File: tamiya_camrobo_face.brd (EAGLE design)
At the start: 60 x 30 mm, 21 parts, among them J4 AUDIO_JACK_3.5MM_KIT

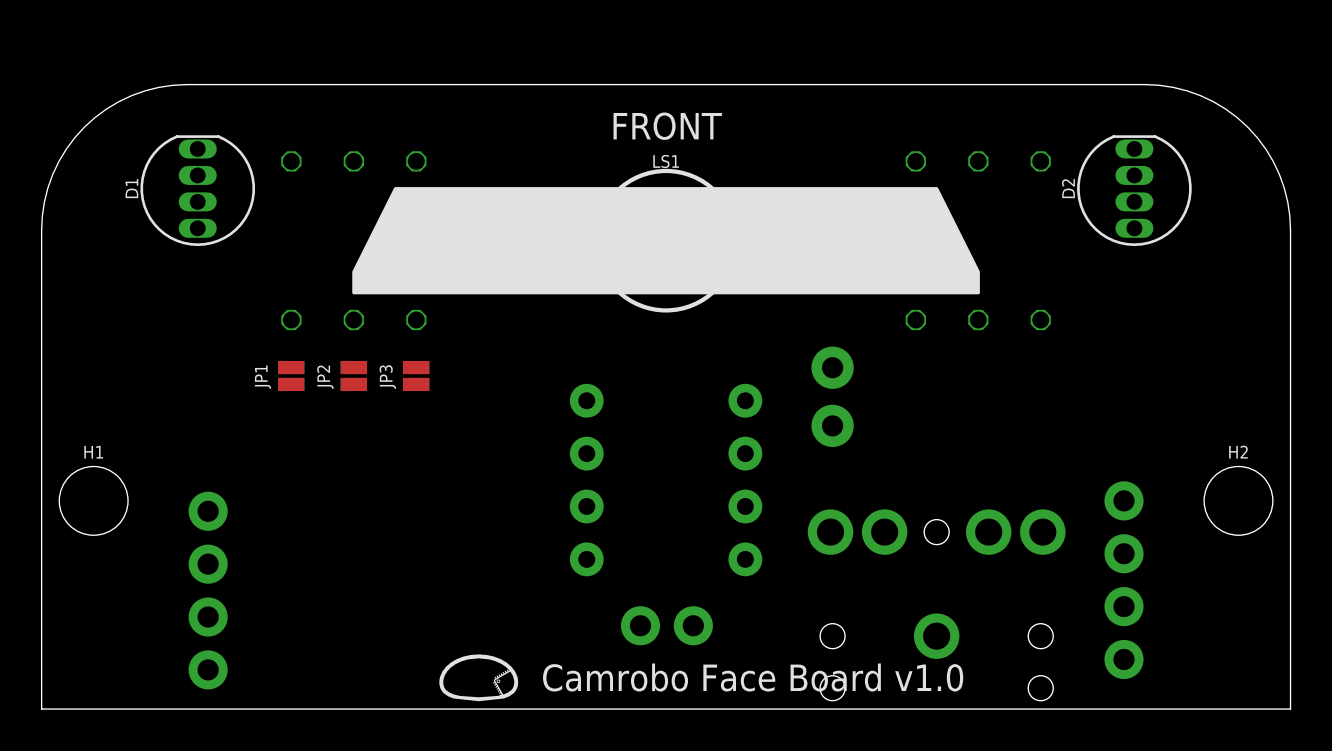
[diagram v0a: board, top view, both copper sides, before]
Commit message: exchange led and amp
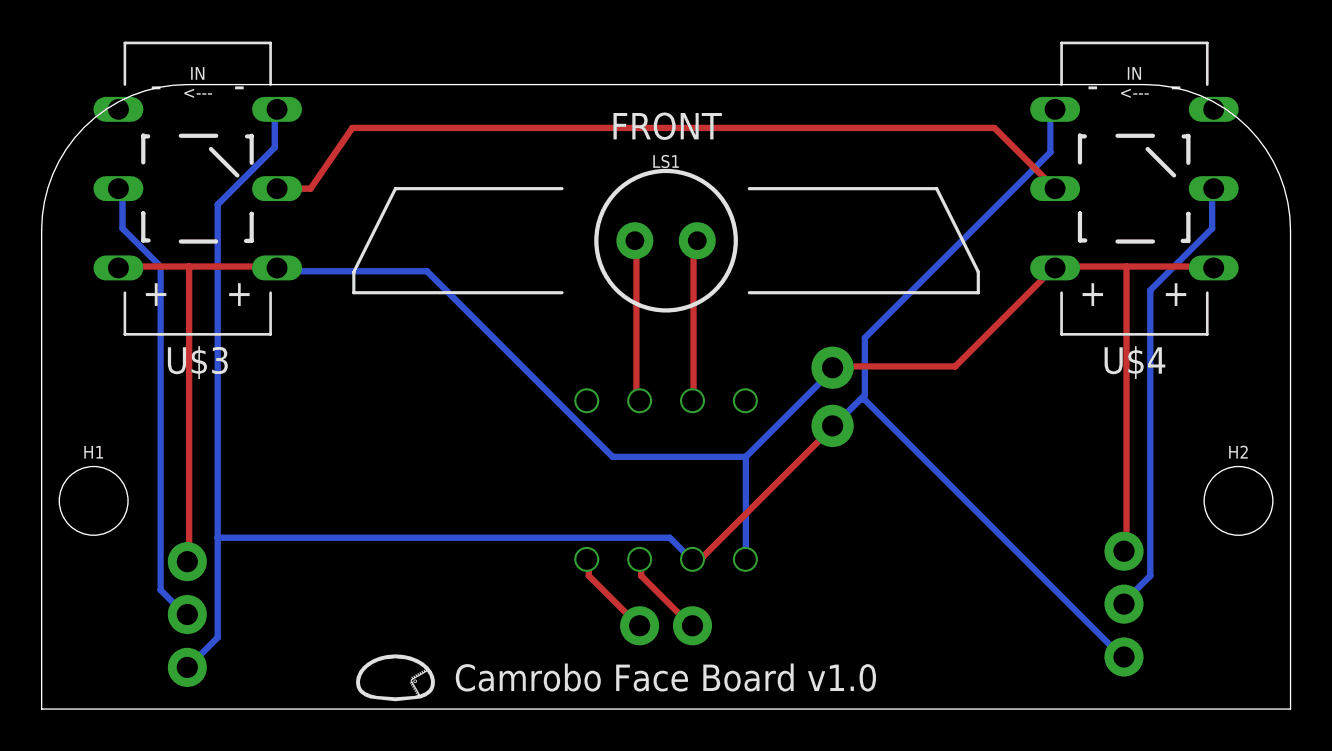
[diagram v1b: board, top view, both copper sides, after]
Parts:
- removed D1, D2: DIFFUSE, SparkFun-LED:LED-RGB-THRU
- removed J1: (no value), SparkFun-Connectors:1X04
- removed J4: AUDIO_JACK_3.5MM_KIT, SparkFun-Connectors:AUDIO-JACK-KIT
- removed JP1, JP2, JP3: JUMPER-SMT_2_NC_PASTE_NO-SILK, SparkFun-Jumpers:SMT-JUMPER_2_NC_PASTE_NO-SILK
- removed R1, R2, R3, R4, R5, R6: (no value), rcl:0204/7
- added J5: (no value), SparkFun-Connectors:1X03
- added U$3, U$4: APA102, Botamochi-sensors:APA102-STRIP-ELEMENT
- J2: device SparkFun-Connectors:1X04 -> SparkFun-Connectors:1X03
- U$1: value AUDIO-AMP-MODULE -> AUDIO-AMP-MODULE_PAM8012; device Botamochi-sensors:DIP8 -> Botamochi-sensors:AE-PAM8012
- moved J2 45.7 mm to (7.00, 2.00), turned to 90 degrees
- moved U$2 4.00 mm to (17.0, 1.50)
- moved J3 2.50 mm to (31.3, 4.00), turned to 0 degrees
- turned U$1 to 90 degrees
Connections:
- removed net +3V3: C1.1, D1.2, D2.2, J1.1, J2.1, U$1.1
- removed net BLU-L: J2.4, JP2.1, R5.1
- removed net BLU-R: J1.4, JP2.2, R2.1
- removed net GRN-L: J2.3, JP3.1, R6.1
- removed net GRN-R: J1.3, JP3.2, R3.1
- removed net N$10: D2.3, R6.2
- removed net N$5: D1.1, R1.2
- removed net N$6: D1.4, R2.2
- removed net N$7: D1.3, R3.2
- removed net N$8: D2.1, R4.2
- removed net N$9: D2.4, R5.2
- removed net RED-L: J2.2, JP1.1, R4.1
- removed net RED-R: J1.2, JP1.2, R1.1
- new net +5V: C1.1, J2.3, J5.3, U$1.P$1, U$3.P$1, U$3.P$6, U$4.P$1, U$4.P$6
- new net DI: J2.2, U$3.P$5
- new net DO: J5.2, U$4.P$2
- new net N$1: U$3.P$2, U$4.P$5
- net AUDIO_IN+: now also U$1.P$3; no longer J4.RING, U$1.3
- net AUDIO_IN-: now also U$1.P$4; no longer J4.SLEEVE, U$1.4
- net AUDIO_OUT+: now also U$1.P$7; no longer U$1.7
- net AUDIO_OUT-: now also U$1.P$6; no longer U$1.6
- net GND: now also J2.1, J5.1, U$1.P$2, U$3.P$3, U$3.P$4, U$4.P$3, U$4.P$4; no longer U$1.2
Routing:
- net GND: track 0.00 -> 98.9 mm
- net +5V: track 0.00 -> 93.2 mm
- net N$1: track 0.00 -> 40.1 mm
- net DI: track 0.00 -> 21.9 mm
- net DO: track 0.00 -> 21.7 mm
- net AUDIO_OUT-: track 0.00 -> 7.83 mm
- net AUDIO_OUT+: track 0.00 -> 7.82 mm
- net AUDIO_IN+: track 0.00 -> 4.26 mm
- net AUDIO_IN-: track 0.00 -> 4.25 mm
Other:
- board text added: "5V"
- board text added: "DI"
- board text added: "DO"
- board text added: "GND"
- board text removed: "3V3"
- board text removed: "B"
- board text removed: "G"
- board text removed: "R"
